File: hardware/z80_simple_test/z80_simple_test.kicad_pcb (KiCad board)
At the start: 2 copper layers, 95 x 100 mm, 35 parts, among them J2 Conn_02x15_Odd_Even, U1 Z84C000XPEG, U2 SRAM_512K8B_DIP_SOP_SOJ, U3 EEPROM_512K8B_DIP, U4 74XX138, U5 Z84C40XPEG

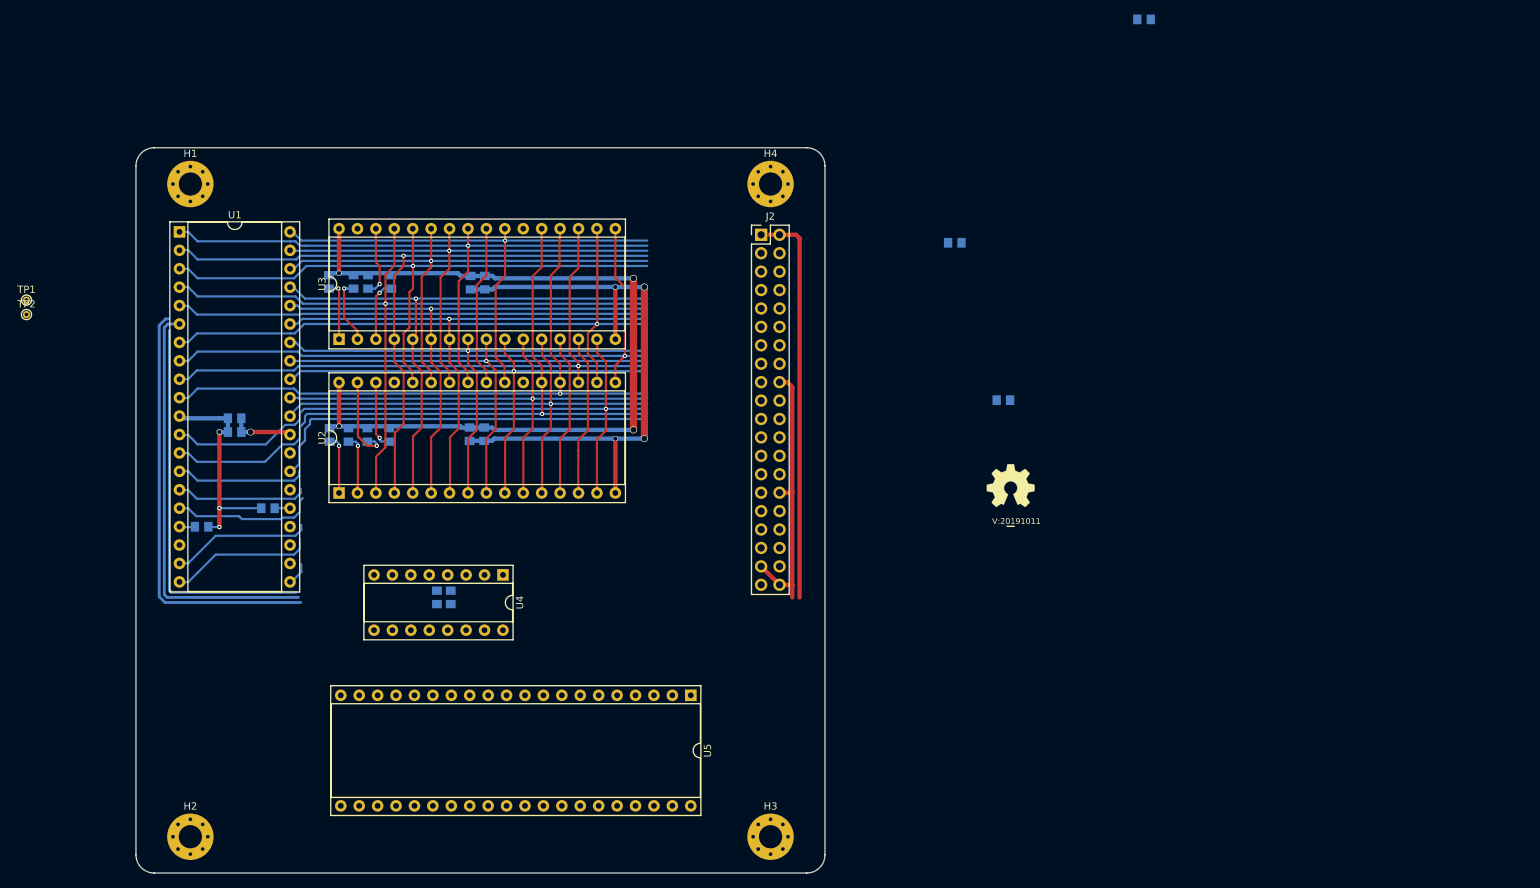
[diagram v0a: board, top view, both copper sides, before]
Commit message: added address selection logic
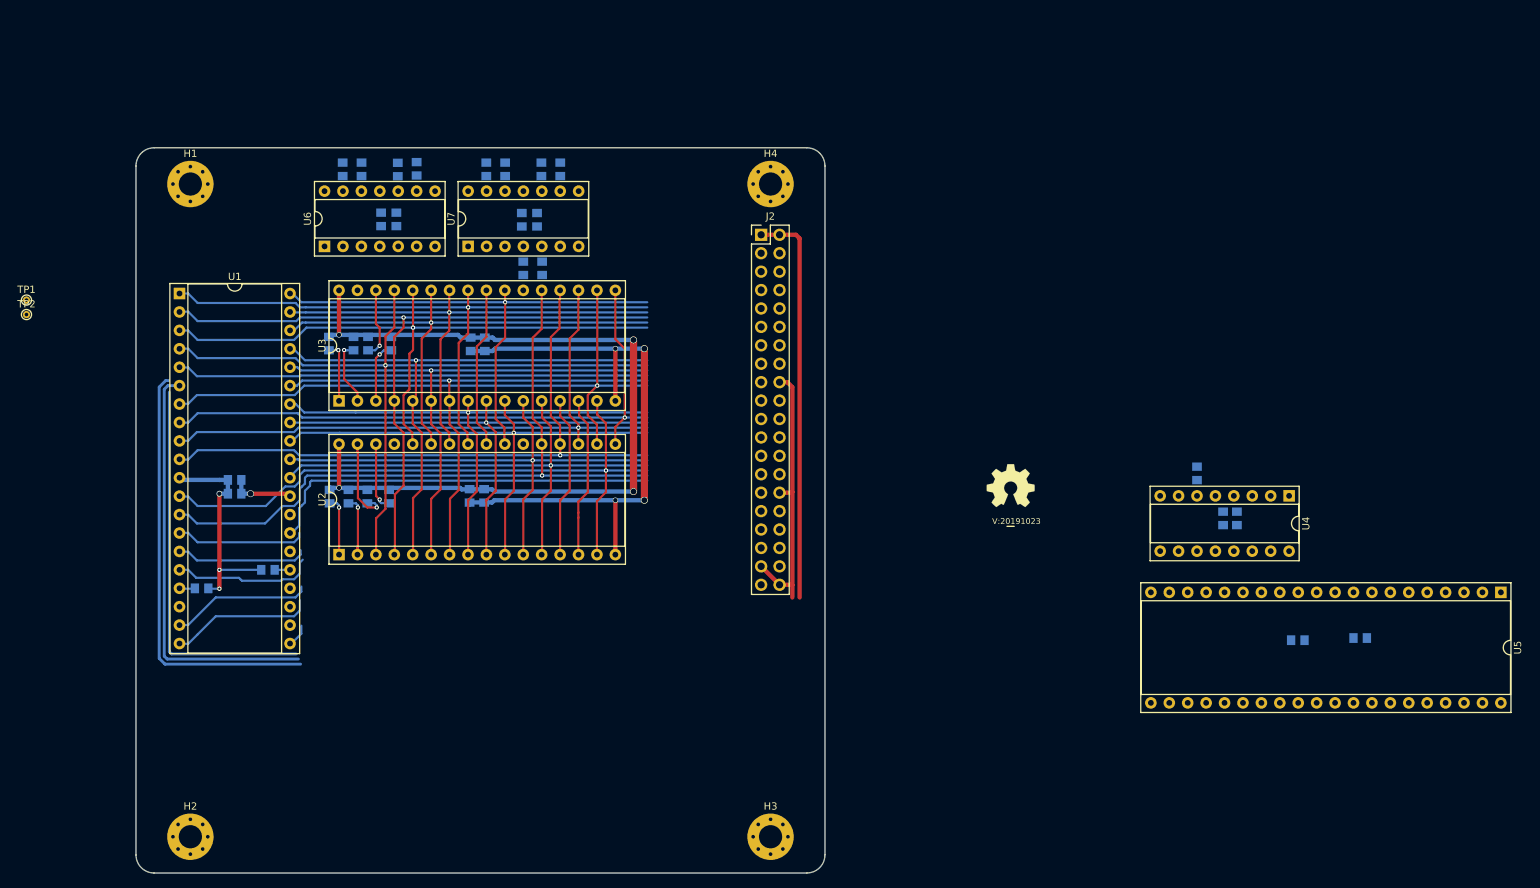
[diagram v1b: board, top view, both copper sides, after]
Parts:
- added C11: 1u, SquantorRcl:C_0805+0603, B.Cu at (157.8, 59.9)
- added C12: 1u, SquantorRcl:C_0805+0603, B.Cu at (138.4, 59.9)
- added C13: 100n, SquantorRcl:C_0805+0603, B.Cu at (136.3, 59.9)
- added C14: 100n, SquantorRcl:C_0805+0603, B.Cu at (155.7, 59.9)
- added R12: 10k, SquantorRcl:C_0805+0603, B.Cu at (155.9, 66.6)
- added R13: 10k, SquantorRcl:C_0805+0603, B.Cu at (158.5, 66.6)
- added R14: 10k, SquantorRcl:C_0805+0603, B.Cu at (131.0, 53.0)
- added R15: 10k, SquantorRcl:C_0805+0603, B.Cu at (133.6, 53.0)
- added R16: 10k, SquantorRcl:C_0805+0603, B.Cu at (138.6, 53.0)
- added R17: 10k, SquantorRcl:C_0805+0603, B.Cu at (141.2, 52.9)
- added R18: 10k, SquantorRcl:C_0805+0603, B.Cu at (150.8, 53.0)
- added R19: 10k, SquantorRcl:C_0805+0603, B.Cu at (153.4, 53.0)
- added R20: 10k, SquantorRcl:C_0805+0603, B.Cu at (158.4, 53.0)
- added R21: 10k, SquantorRcl:C_0805+0603, B.Cu at (161.0, 53.0)
- added U6: 74XX32, Package_DIP:DIP-14_W7.62mm_Socket, F.Cu at (128.5, 63.6)
- added U7: 74XX00, Package_DIP:DIP-14_W7.62mm_Socket, F.Cu at (148.3, 63.6)
- N2: value V:20191011 -> V:20191023
- moved U5 112.6 mm to (290.7, 111.3)
- moved C7 108.9 mm to (252.4, 101.1)
- moved C8 108.9 mm to (254.3, 101.1)
- moved U4 108.9 mm to (261.5, 98.0)
- moved C10 90.4 mm to (271.3, 117.6)
- moved C9 52.4 mm to (262.7, 117.9)
- moved R2 46.1 mm to (248.8, 94.9), turned to 90 degrees
- moved C1 8.50 mm to (116.1, 95.8)
- moved C2 8.50 mm to (116.1, 97.7)
- moved C3 8.50 mm to (148.5, 98.0)
- moved C4 8.50 mm to (150.5, 98.0)
- moved C5 8.50 mm to (150.6, 77.1)
- moved C6 8.50 mm to (148.7, 77.1)
- moved R1 8.50 mm to (120.7, 108.2)
- moved R10 8.50 mm to (134.5, 77.0)
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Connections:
- U2 pad 22: (no net) -> /!RAM_CE
- U3 pad 22: (no net) -> /A15

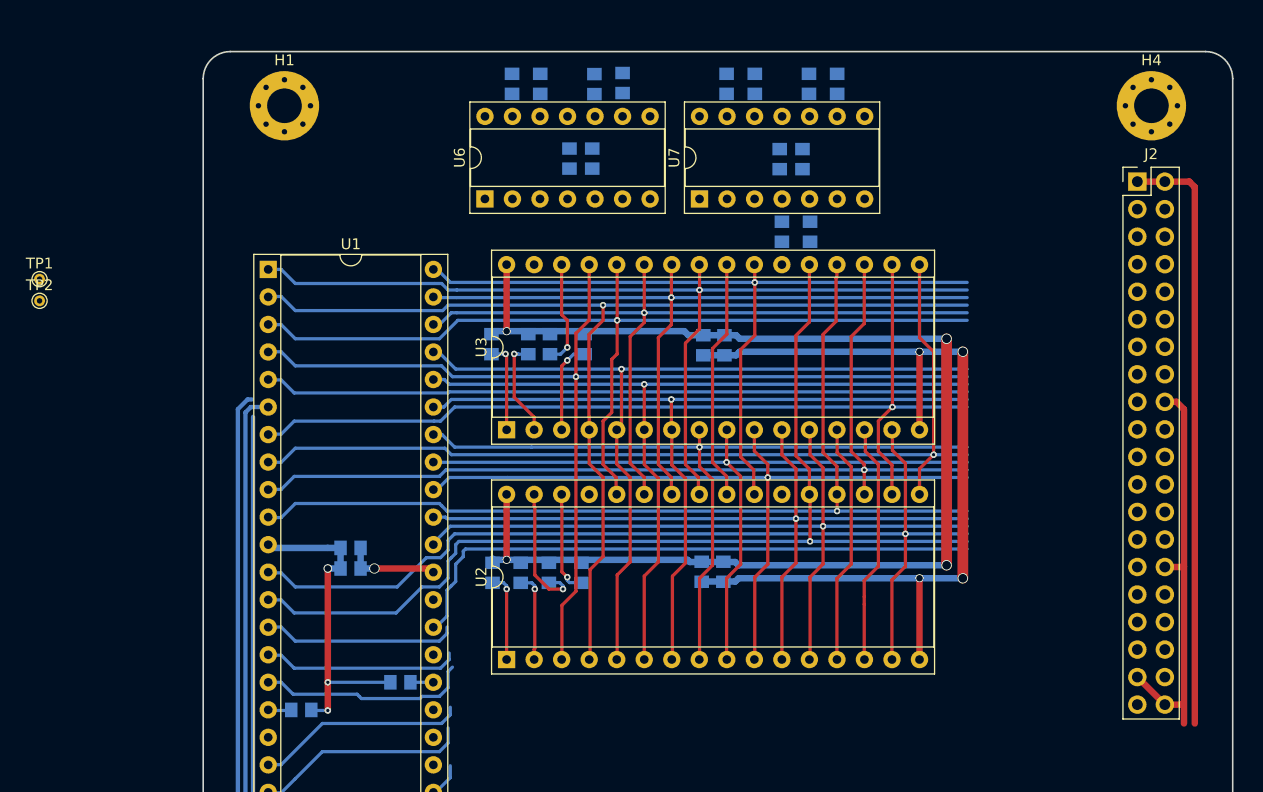
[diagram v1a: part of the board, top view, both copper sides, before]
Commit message: added barreljack to PCB
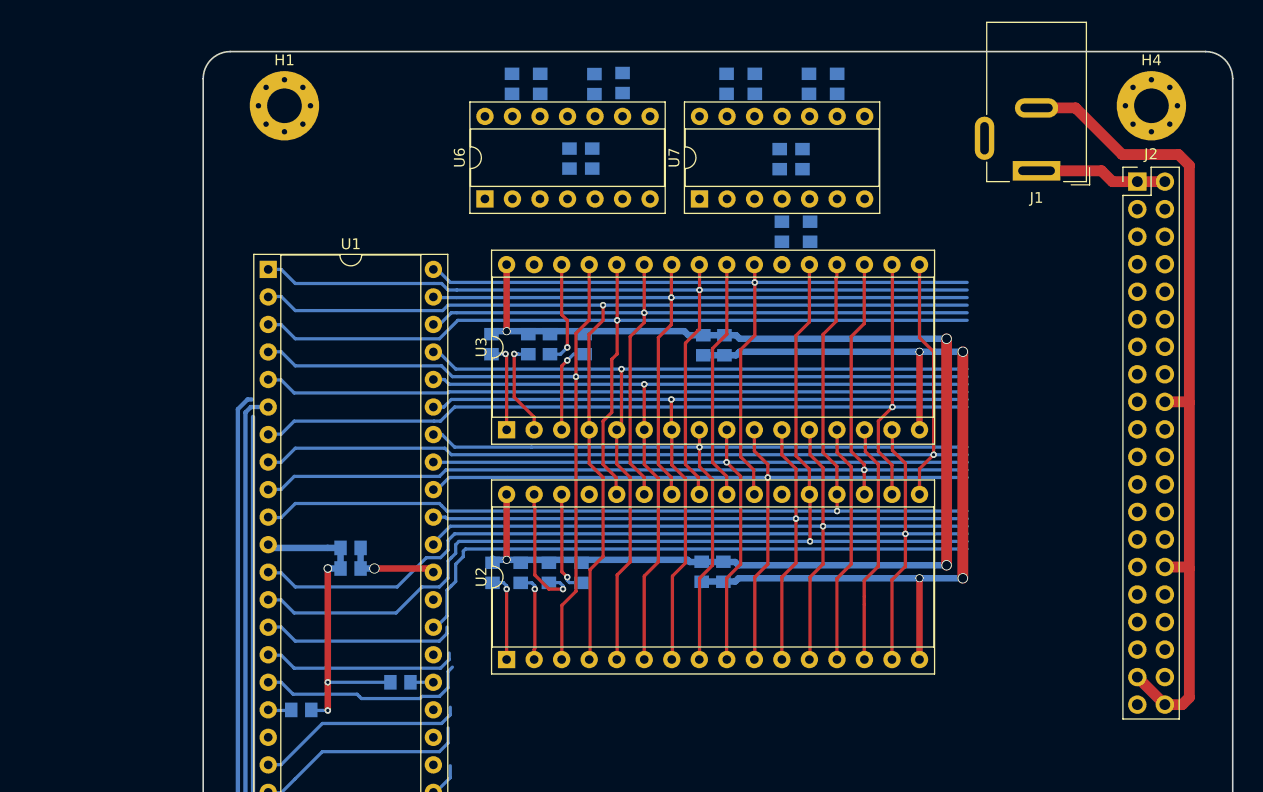
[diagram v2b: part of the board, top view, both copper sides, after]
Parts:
- removed TP1, TP2: testpad, TestPoint:TestPoint_THTPad_D1.0mm_Drill0.5mm
- added J1: Barrel_Jack_Switch, Connector_BarrelJack:BarrelJack_Wuerth_6941xx301002, F.Cu at (179.4, 61.0)
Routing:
- net /VDD: track 203.0 -> 160.2 mm
- net /VSS: track 243.3 -> 281.3 mm
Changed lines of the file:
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@@
     (thickness 1.6)
     (drawings 10)
-    (tracks 545)
+    (tracks 549)
     (zones 0)
-    (modules 51)
+    (modules 50)
     (nets 62)
   )
@@
   )
   (setup
-    (last_trace_width 0.2)
+    (last_trace_width 1)
     (user_trace_width 0.15)
     (user_trace_width 0.2)
@@
     (add_net /D7)
     (add_net /SEL_SIO)
+    (add_net "Net-(J1-Pad3)")
     (add_net "Net-(R1-Pad2)")
     (add_net "Net-(R12-Pad1)")
@@
     (add_net /VDD)
     (add_net /VSS)
+  )
+  (module Connector_BarrelJack:BarrelJack_Wuerth_6941xx301002 (layer F.Cu)
+    (at 179.4 61 180)
+    (descr "Wuerth electronics barrel jack connector (5.5mm outher diameter, inner diameter 2.05mm or 2.55mm depending on exact order number), See: http://katalog.we-online.de/em/datasheet/6941xx301002.pdf")
+    (tags "connector barrel jack")
+    (fp_text reference J1 (at 0 -2.5) (layer F.SilkS)
+      (effects (font (size 1 1) (thickness 0.15)))
+    )
+    (fp_text value Barrel_Jack_Switch (at 0 15.5) (layer F.Fab)
+      (effects (font (size 1 1) (thickness 0.15)))
+    )
+    (fp_line (start -4.6 -1) (end -2.5 -1) (layer F.SilkS) (width 0.12))
+    (fp_line (start 6.2 0.5) (end 5 0.5) (layer F.CrtYd) (width 0.05))
+    (fp_line (start 6.2 5.5) (end 5 5.5) (layer F.CrtYd) (width 0.05))
+    (fp_line (start 6.2 0.5) (end 6.2 5.5) (layer F.CrtYd) (width 0.05))
+    (fp_line (start 5 0.5) (end 5 -1.4) (layer F.CrtYd) (width 0.05))
+    (fp_line (start -5 14.1) (end 5 14.1) (layer F.CrtYd) (width 0.05))
+    (fp_line (start -5 -1.4) (end -5 14.1) (layer F.CrtYd) (width 0.05))
+    (fp_line (start 5 -1.4) (end -5 -1.4) (layer F.CrtYd) (width 0.05))
+    (fp_line (start -4.9 -1.3) (end -4.9 0.3) (layer F.SilkS) (width 0.12))
+    (fp_line (start -3.2 -1.3) (end -4.9 -1.3) (layer F.SilkS) (width 0.12))
+    (fp_line (start 4.6 -1) (end 4.6 0.8) (layer F.SilkS) (width 0.12))
+    (fp_line (start 2.5 -1) (end 4.6 -1) (layer F.SilkS) (width 0.12))
+    (fp_line (start -4.6 13.7) (end -4.6 -1) (layer F.SilkS) (width 0.12))
+    (fp_line (start 4.6 13.7) (end -4.6 13.7) (layer F.SilkS) (width 0.12))
+    (fp_text user %R (at 0 7.5) (layer F.Fab)
+      (effects (font (size 1 1) (thickness 0.15)))
+    )
+    (fp_line (start -4.5 13.6) (end -4.5 0.1) (layer F.Fab) (width 0.1))
+    (fp_line (start 4.5 13.6) (end -4.5 13.6) (layer F.Fab) (width 0.1))
+    (fp_line (start 4.5 -0.9) (end 4.5 13.6) (layer F.Fab) (width 0.1))
+    (fp_line (start 4.5 -0.9) (end -3.5 -0.9) (layer F.Fab) (width 0.1))
+    (fp_line (start -4.5 0.1) (end -3.5 -0.9) (layer F.Fab) (width 0.1))
+    (fp_line (start 4.6 5.2) (end 4.6 13.7) (layer F.SilkS) (width 0.12))
+    (fp_line (start 5 14.1) (end 5 5.5) (layer F.CrtYd) (width 0.05))
+    (pad 1 thru_hole rect (at 0 0 180) (size 4.4 1.8) (drill oval 3.4 0.8) (layers *.Cu *.Mask)
+      (net 2 /VDD))
+    (pad 2 thru_hole oval (at 0 5.8 180) (size 4 1.8) (drill oval 3 0.8) (layers *.Cu *.Mask)
+      (net 1 /VSS))
+    (pad 3 thru_hole oval (at 4.8 3 270) (size 4 1.8) (drill oval 3 0.8) (layers *.Cu *.Mask))
+    (model ${KISYS3DMOD}/Connector_BarrelJack.3dshapes/BarrelJack_Wuerth_6941xx301002.wrl
+      (at (xyz 0 0 0))
+      (scale (xyz 1 1 1))
+      (rotate (xyz 0 0 0))
+    )
   )
   (module Package_DIP:DIP-14_W7.62mm_Socket (layer F.Cu)
@@
       (rotate (xyz 0 0 0))
     )
-  )
-  (module TestPoint:TestPoint_THTPad_D1.0mm_Drill0.5mm (layer F.Cu)
-    (at 87.4 73)
-    (descr "THT pad as test Point, diameter 1.0mm, hole diameter 0.5mm")
-    (tags "test point THT pad")
-    (attr virtual)
-    (fp_text reference TP2 (at 0 -1.448) (layer F.SilkS)
-      (effects (font (size 1 1) (thickness 0.15)))
-    )
-    (fp_text value testpad (at 0 1.55) (layer F.Fab)
-      (effects (font (size 1 1) (thickness 0.15)))
-    )
-    (fp_circle (center 0 0) (end 0 0.7) (layer F.SilkS) (width 0.12))
-    (fp_circle (center 0 0) (end 1 0) (layer F.CrtYd) (width 0.05))
-    (fp_text user %R (at 0 -1.45) (layer F.Fab)
-      (effects (font (size 1 1) (thickness 0.15)))
-    )
-    (pad 1 thru_hole circle (at 0 0) (size 1 1) (drill 0.5) (layers *.Cu *.Mask)
-      (net 2 /VDD))
-  )
-  (module TestPoint:TestPoint_THTPad_D1.0mm_Drill0.5mm (layer F.Cu)
-    (at 87.4 71)
-    (descr "THT pad as test Point, diameter 1.0mm, hole diameter 0.5mm")
-    (tags "test point THT pad")
-    (attr virtual)
-    (fp_text reference TP1 (at 0 -1.448) (layer F.SilkS)
-      (effects (font (size 1 1) (thickness 0.15)))
-    )
-    (fp_text value testpad (at 0 1.55) (layer F.Fab)
-      (effects (font (size 1 1) (thickness 0.15)))
-    )
-    (fp_circle (center 0 0) (end 0 0.7) (layer F.SilkS) (width 0.12))
-    (fp_circle (center 0 0) (end 1 0) (layer F.CrtYd) (width 0.05))
-    (fp_text user %R (at 0 -1.45) (layer F.Fab)
-      (effects (font (size 1 1) (thickness 0.15)))
-    )
-    (pad 1 thru_hole circle (at 0 0) (size 1 1) (drill 0.5) (layers *.Cu *.Mask)
-      (net 1 /VSS))
   )
   (module MountingHole:MountingHole_3.2mm_M3_Pad_Via locked (layer F.Cu)
@@
   (segment (start 152 77.7) (end 151.675 78.025) (width 0.6) (layer B.Cu) (net 1))
   (segment (start 151.675 78.025) (end 150.6 78.025) (width 0.6) (layer B.Cu) (net 1))
-  (via (at 168.6 77.7) (size 0.75) (drill 0.6) (layers F.Cu B.Cu) (net 1) (status 1000000))
+  (via (at 168.6 77.7) (size 0.75) (drill 0.6) (layers F.Cu B.Cu) (net 1))
   (segment (start 168.6 77.7) (end 152 77.7) (width 0.6) (layer B.Cu) (net 1))
   (segment (start 151.6 98.9) (end 148.825 98.9) (width 0.6) (layer B.Cu) (net 1))
@@
   (segment (start 172.6 98.6) (end 168.6 98.6) (width 0.6) (layer B.Cu) (net 1))
   (via (at 172.6 98.6) (size 0.95) (drill 0.8) (layers F.Cu B.Cu) (net 1))
-  (segment (start 191.24 82.32) (end 192.32 82.32) (width 0.6) (layer F.Cu) (net 1))
-  (segment (start 192.32 82.32) (end 193 83) (width 0.6) (layer F.Cu) (net 1))
-  (segment (start 192.96 110.26) (end 193 110.3) (width 0.6) (layer F.Cu) (net 1))
-  (segment (start 191.24 110.26) (end 192.96 110.26) (width 0.6) (layer F.Cu) (net 1))
-  (segment (start 193 110.3) (end 193 112) (width 0.6) (layer F.Cu) (net 1))
-  (segment (start 188.7 107.72) (end 191.24 110.26) (width 0.6) (layer F.Cu) (net 1))
-  (segment (start 192.94 97.56) (end 193 97.5) (width 0.6) (layer F.Cu) (net 1))
-  (segment (start 191.24 97.56) (end 192.94 97.56) (width 0.6) (layer F.Cu) (net 1))
-  (segment (start 193 83) (end 193 97.5) (width 0.6) (layer F.Cu) (net 1))
-  (segment (start 193 97.5) (end 193 110.3) (width 0.6) (layer F.Cu) (net 1))
+  (segment (start 192.84 110.26) (end 193.5 109.6) (width 1) (layer F.Cu) (net 1))
+  (segment (start 191.24 110.26) (end 192.84 110.26) (width 1) (layer F.Cu) (net 1))
+  (segment (start 192.5 59.5) (end 187.3 59.5) (width 1) (layer F.Cu) (net 1))
+  (segment (start 193.5 60.5) (end 192.5 59.5) (width 1) (layer F.Cu) (net 1))
+  (segment (start 183 55.2) (end 179.4 55.2) (width 1) (layer F.Cu) (net 1))
+  (segment (start 187.3 59.5) (end 183 55.2) (width 1) (layer F.Cu) (net 1))
+  (segment (start 193.36 97.56) (end 193.5 97.7) (width 1) (layer F.Cu) (net 1))
+  (segment (start 191.24 97.56) (end 193.36 97.56) (width 1) (layer F.Cu) (net 1))
+  (segment (start 193.5 109.6) (end 193.5 97.7) (width 1) (layer F.Cu) (net 1))
+  (segment (start 193.42 82.32) (end 193.5 82.4) (width 1) (layer F.Cu) (net 1))
+  (segment (start 191.24 82.32) (end 193.42 82.32) (width 1) (layer F.Cu) (net 1))
+  (segment (start 193.5 97.7) (end 193.5 82.4) (width 1) (layer F.Cu) (net 1))
+  (segment (start 193.5 82.4) (end 193.5 60.5) (width 1) (layer F.Cu) (net 1))
+  (segment (start 188.7 107.72) (end 191.24 110.26) (width 1) (layer F.Cu) (net 1))
   (segment (start 148.65 76.175) (end 150.6 76.175) (width 0.6) (layer B.Cu) (net 2))
   (segment (start 130.5 96.9) (end 130.5 90.86) (width 0.6) (layer F.Cu) (net 2))
@@
   (segment (start 114 95.8) (end 115.175 95.8) (width 0.6) (layer B.Cu) (net 2))
   (segment (start 108.8 95.8) (end 114 95.8) (width 0.6) (layer B.Cu) (net 2))
-  (segment (start 188.7 62) (end 191.24 62) (width 0.6) (layer F.Cu) (net 2))
-  (segment (start 191.24 62) (end 193.5 62) (width 0.6) (layer F.Cu) (net 2))
-  (segment (start 193.5 62) (end 194 62.5) (width 0.6) (layer F.Cu) (net 2))
-  (segment (start 194 62.5) (end 194 112) (width 0.6) (layer F.Cu) (net 2))
+  (segment (start 191.24 62) (end 188.7 62) (width 1) (layer F.Cu) (net 2))
+  (segment (start 188.7 62) (end 186.4 62) (width 1) (layer F.Cu) (net 2))
+  (segment (start 185.4 61) (end 179.4 61) (width 1) (layer F.Cu) (net 2))
+  (segment (start 186.4 62) (end 185.4 61) (width 1) (layer F.Cu) (net 2))
   (segment (start 123.74 70.1) (end 124.1 70.1) (width 0.3) (layer B.Cu) (net 3))
   (segment (start 124.1 70.1) (end 125.1 71.1) (width 0.3) (layer B.Cu) (net 3))

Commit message: selection logic placement
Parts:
- moved R14 14.3 mm to (126.0, 66.4), turned to 90 degrees
- moved R15 14.3 mm to (128.6, 66.4), turned to 90 degrees
- moved C12 11.4 mm to (127.0, 59.6)
- moved C13 11.2 mm to (125.1, 59.6)
- moved C11 11.0 mm to (146.8, 59.6)
- moved C14 10.8 mm to (144.9, 59.6)
- moved U7 10.1 mm to (138.2, 63.4)
- moved R12 10.1 mm to (145.8, 66.4)
- moved R13 10.1 mm to (148.4, 66.4)
- moved R16 10.1 mm to (128.5, 52.8)
- moved U6 10.1 mm to (118.4, 63.4)
- moved R18 10.1 mm to (140.7, 52.8)
- moved R19 10.1 mm to (143.3, 52.8)
- moved R20 10.1 mm to (148.3, 52.8)
- moved R21 10.1 mm to (150.9, 52.8)
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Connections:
- R14 pad 1: /VDD -> /VSS
- R15 pad 1: /VDD -> /VSS
- U6 pad 11: (no net) -> /!MREQ
- U6 pad 12: Net-(R15-Pad2) -> /!MEM_RD
- U6 pad 13: Net-(R14-Pad2) -> /!RD
- U6 pad 4: /!MREQ -> Net-(R14-Pad2)
- U6 pad 5: /!RD -> Net-(R15-Pad2)
- U6 pad 6: /!MEM_RD -> (no net)
- U6 pad 7: /VSS -> (no net)
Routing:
- net /VDD: track 160.2 -> 233.8 mm, vias 7 -> 9
- net /VSS: track 281.3 -> 336.3 mm, vias 5 -> 7
- net Net-(R17-Pad2): track 0.00 -> 2.16 mm
- net Net-(R13-Pad1): track 0.00 -> 2.12 mm
- net Net-(R12-Pad1): track 0.00 -> 2.11 mm
- net Net-(R20-Pad2): track 0.00 -> 2.10 mm
- net Net-(R18-Pad2): track 0.00 -> 2.10 mm
- net Net-(R15-Pad2): track 0.00 -> 2.09 mm
- net Net-(R19-Pad2): track 0.00 -> 2.09 mm
- net Net-(R14-Pad2): track 0.00 -> 2.08 mm
- net Net-(R21-Pad2): track 0.00 -> 2.08 mm
- net Net-(R16-Pad2): track 0.00 -> 2.08 mm
